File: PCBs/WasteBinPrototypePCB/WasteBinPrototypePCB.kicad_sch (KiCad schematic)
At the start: 31 parts, among them J1 Jack-DC 12V, J2 Conn_01x10_Male, J3 Conn_01x06_Male, J4 SM04B-SRSS-TB(LF)(SN), Q1 MMBT3904, Q2 IRL540NSTRLPBF, U1 PC817, U2 TLV1117-50, U3 ESP32-C3-DEVKITC-02, U4 A1301EUA-T

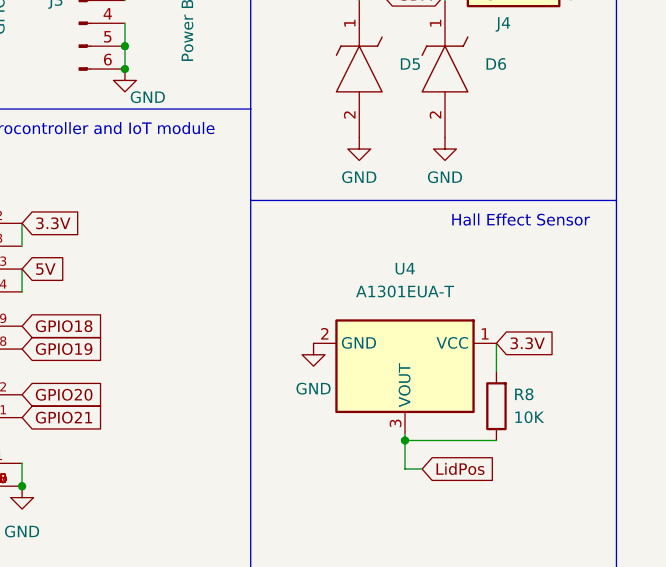
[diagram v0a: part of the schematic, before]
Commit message: footprints assigned to each component
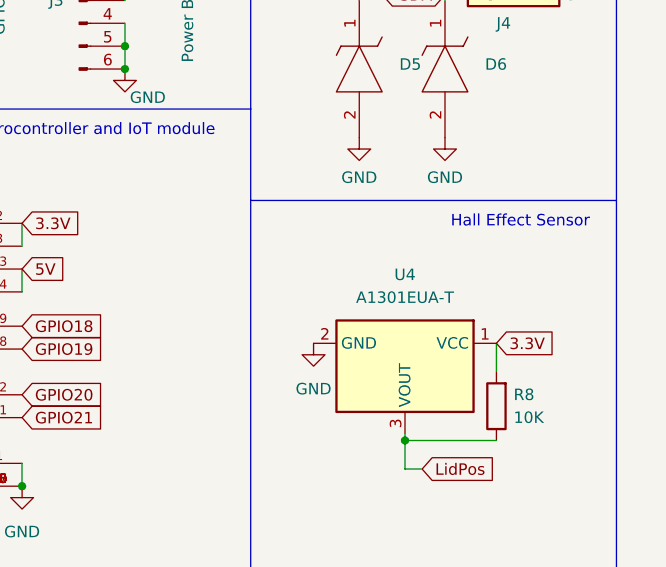
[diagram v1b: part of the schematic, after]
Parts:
- D2: footprint (none) -> LED_SMD:LED_0805_2012Metric_Pad1.15x1.40mm_HandSolder
- D4: footprint (none) -> Diode_SMD:D_0805_2012Metric_Pad1.15x1.40mm_HandSolder; Purpose (none) -> Reverse voltage protection
- J2: footprint (none) -> Connector_PinSocket_2.54mm:PinSocket_1x10_P2.54mm_Vertical
- J3: footprint (none) -> Connector_PinSocket_2.54mm:PinSocket_1x06_P2.54mm_Vertical
- LS1: footprint CMT752580SMTTR -> LED_SMD:LED_0805_2012Metric_Pad1.15x1.40mm_HandSolder
- Q2: footprint IRF2804STRLPBF -> SamacSys_Parts:IRF2804STRLPBF
- R1, R2, R3, R4, R5, R6, R7, R8: footprint (none) -> Resistor_SMD:R_0805_2012Metric_Pad1.20x1.40mm_HandSolder
- U2: footprint (none) -> SamacSys_Parts:SOT230P700X180-4N
- U4: footprint (none) -> Connector_PinSocket_2.54mm:PinSocket_1x03_P2.54mm_Vertical
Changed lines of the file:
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@@
       (effects (font (size 1.27 1.27)) (justify left))
     )
-    (property "Footprint" "IRF2804STRLPBF" (id 2) (at 41.275 45.085 0)
+    (property "Footprint" "SamacSys_Parts:IRF2804STRLPBF" (id 2) (at 41.275 45.085 0)
       (effects (font (size 1.27 1.27)) (justify left) hide)
     )
@@
       (effects (font (size 1.27 1.27)) hide)
     )
-    (property "Footprint" "" (id 2) (at 171.45 29.21 0)
+    (property "Footprint" "Connector_PinSocket_2.54mm:PinSocket_1x06_P2.54mm_Vertical" (id 2) (at 171.45 29.21 0)
       (effects (font (size 1.27 1.27)) hide)
     )
@@
       (effects (font (size 1.27 1.27)) (justify left))
     )
-    (property "Footprint" "" (id 2) (at 52.197 47.625 90)
+    (property "Footprint" "Resistor_SMD:R_0805_2012Metric_Pad1.20x1.40mm_HandSolder" (id 2) (at 52.197 47.625 90)
       (effects (font (size 1.27 1.27)) hide)
     )
@@
       (effects (font (size 1.27 1.27)) (justify right))
     )
-    (property "Footprint" "" (id 2) (at 219.583 74.295 90)
+    (property "Footprint" "Resistor_SMD:R_0805_2012Metric_Pad1.20x1.40mm_HandSolder" (id 2) (at 219.583 74.295 90)
       (effects (font (size 1.27 1.27)) hide)
     )
@@
       (effects (font (size 1.27 1.27)) (justify left))
     )
-    (property "Footprint" "" (id 2) (at 67.31 47.625 0)
+    (property "Footprint" "Diode_SMD:D_0805_2012Metric_Pad1.15x1.40mm_HandSolder" (id 2) (at 67.31 47.625 0)
       (effects (font (size 1.27 1.27)) hide)
     )
     (property "Datasheet" "~" (id 3) (at 67.31 47.625 0)
+      (effects (font (size 1.27 1.27)) hide)
+    )
+    (property "Purpose" "Reverse voltage protection " (id 4) (at 67.31 47.625 0)
       (effects (font (size 1.27 1.27)) hide)
     )
@@
     (property "Reference" "R5" (id 0) (at 59.69 38.1 90))
     (property "Value" "100" (id 1) (at 59.69 40.64 90))
-    (property "Footprint" "" (id 2) (at 59.69 45.593 90)
+    (property "Footprint" "Resistor_SMD:R_0805_2012Metric_Pad1.20x1.40mm_HandSolder" (id 2) (at 59.69 45.593 90)
       (effects (font (size 1.27 1.27)) hide)
     )
@@
       (effects (font (size 1.27 1.27)) (justify right))
     )
-    (property "Footprint" "" (id 2) (at 46.863 72.39 90)
+    (property "Footprint" "Resistor_SMD:R_0805_2012Metric_Pad1.20x1.40mm_HandSolder" (id 2) (at 46.863 72.39 90)
       (effects (font (size 1.27 1.27)) hide)
     )
@@
       (effects (font (size 1.27 1.27)) (justify left))
     )
-    (property "Footprint" "" (id 2) (at 65.532 24.765 90)
+    (property "Footprint" "Resistor_SMD:R_0805_2012Metric_Pad1.20x1.40mm_HandSolder" (id 2) (at 65.532 24.765 90)
       (effects (font (size 1.27 1.27)) hide)
     )
@@
     (property "Reference" "R1" (id 0) (at 41.275 78.105 90))
     (property "Value" "1K" (id 1) (at 41.275 80.645 90))
-    (property "Footprint" "" (id 2) (at 41.275 85.598 90)
+    (property "Footprint" "Resistor_SMD:R_0805_2012Metric_Pad1.20x1.40mm_HandSolder" (id 2) (at 41.275 85.598 90)
       (effects (font (size 1.27 1.27)) hide)
     )
@@
       (effects (font (size 1.27 1.27)) (justify left))
     )
-    (property "Footprint" "" (id 2) (at 43.307 29.21 90)
+    (property "Footprint" "Resistor_SMD:R_0805_2012Metric_Pad1.20x1.40mm_HandSolder" (id 2) (at 43.307 29.21 90)
       (effects (font (size 1.27 1.27)) hide)
     )
@@
     (property "Reference" "LS1" (id 0) (at 67.945 63.5 0))
     (property "Value" "CMT-7525-80-SMT-TR" (id 1) (at 67.945 66.04 0))
-    (property "Footprint" "CMT752580SMTTR" (id 2) (at 78.105 69.215 0)
+    (property "Footprint" "LED_SMD:LED_0805_2012Metric_Pad1.15x1.40mm_HandSolder" (id 2) (at 78.105 69.215 0)
       (effects (font (size 1.27 1.27)) (justify left) hide)
     )
@@
       (effects (font (size 1.27 1.27)) hide)
     )
-    (property "Footprint" "" (id 2) (at 146.05 26.67 0)
+    (property "Footprint" "Connector_PinSocket_2.54mm:PinSocket_1x10_P2.54mm_Vertical" (id 2) (at 146.05 26.67 0)
       (effects (font (size 1.27 1.27)) hide)
     )
@@
   (symbol (lib_id "Sensor_Magnetic:A1301EUA-T") (at 207.645 69.85 270) (unit 1)
     (in_bom yes) (on_board yes) (fields_autoplaced)
-    (property "Reference" "U4" (id 0) (at 207.645 59.055 90))
-    (property "Value" "A1301EUA-T" (id 1) (at 207.645 61.595 90))
-    (property "Footprint" "" (id 2) (at 198.755 69.85 0)
+    (property "Reference" "U4" (id 0) (at 207.645 59.69 90))
+    (property "Value" "A1301EUA-T" (id 1) (at 207.645 62.23 90))
+    (property "Footprint" "Connector_PinSocket_2.54mm:PinSocket_1x03_P2.54mm_Vertical" (id 2) (at 198.755 69.85 0)
       (effects (font (size 1.27 1.27) italic) (justify left) hide)
     )
@@
     (property "Reference" "U2" (id 0) (at 120.65 17.145 0))
     (property "Value" "TLV1117-50" (id 1) (at 120.65 19.685 0))
-    (property "Footprint" "" (id 2) (at 120.65 24.13 0)
+    (property "Footprint" "SamacSys_Parts:SOT230P700X180-4N" (id 2) (at 120.65 24.13 0)
       (effects (font (size 1.27 1.27)) hide)
     )
@@
       (effects (font (size 1.27 1.27)) (justify right))
     )
-    (property "Footprint" "" (id 2) (at 45.085 20.32 0)
+    (property "Footprint" "LED_SMD:LED_0805_2012Metric_Pad1.15x1.40mm_HandSolder" (id 2) (at 45.085 20.32 0)
       (effects (font (size 1.27 1.27)) hide)
     )
@@
     (property "Reference" "R7" (id 0) (at 86.36 29.21 90))
     (property "Value" "1K" (id 1) (at 86.36 31.75 90))
-    (property "Footprint" "" (id 2) (at 86.36 37.338 90)
+    (property "Footprint" "Resistor_SMD:R_0805_2012Metric_Pad1.20x1.40mm_HandSolder" (id 2) (at 86.36 37.338 90)
       (effects (font (size 1.27 1.27)) hide)
     )
@@
     )
     (path "/f387ffcc-26b6-418e-82fe-9f2886ad1d96"
-      (reference "D2") (unit 1) (value "LED") (footprint "")
+      (reference "D2") (unit 1) (value "LED") (footprint "LED_SMD:LED_0805_2012Metric_Pad1.15x1.40mm_HandSolder")
     )
     (path "/3b6822c2-ef43-441b-ada3-a919003dfb41"
@@
     )
     (path "/2daceb28-157a-44a8-abe7-ecdcfa40433f"
-      (reference "D4") (unit 1) (value "D") (footprint "")
+      (reference "D4") (unit 1) (value "D") (footprint "Diode_SMD:D_0805_2012Metric_Pad1.15x1.40mm_HandSolder")
     )
     (path "/de6b862e-7ecd-43af-9a8b-58b048cb163f"
@@
     )
     (path "/ba6425fc-a624-41b4-91aa-0f0a86e87413"
-      (reference "J2") (unit 1) (value "Conn_01x10_Male") (footprint "")
+      (reference "J2") (unit 1) (value "Conn_01x10_Male") (footprint "Connector_PinSocket_2.54mm:PinSocket_1x10_P2.54mm_Vertical")
     )
     (path "/1886b725-a5c3-4ddc-8a4b-0787c5600503"
-      (reference "J3") (unit 1) (value "Conn_01x06_Male") (footprint "")
+      (reference "J3") (unit 1) (value "Conn_01x06_Male") (footprint "Connector_PinSocket_2.54mm:PinSocket_1x06_P2.54mm_Vertical")
     )
     (path "/48eea9cc-6ff2-4ff5-8e23-5348d769bac2"
@@
     )
     (path "/9af62221-658d-49f1-9d88-b604899cb68f"
-      (reference "LS1") (unit 1) (value "CMT-7525-80-SMT-TR") (footprint "CMT752580SMTTR")
+      (reference "LS1") (unit 1) (value "CMT-7525-80-SMT-TR") (footprint "LED_SMD:LED_0805_2012Metric_Pad1.15x1.40mm_HandSolder")
     )
     (path "/6cbf8465-a06f-4c9b-9f77-203331441ebb"
@@
     )
     (path "/00039052-8388-45e9-8681-1233f0361ca2"
-      (reference "Q2") (unit 1) (value "IRL540NSTRLPBF") (footprint "IRF2804STRLPBF")
+      (reference "Q2") (unit 1) (value "IRL540NSTRLPBF") (footprint "SamacSys_Parts:IRF2804STRLPBF")
     )
     (path "/8a915310-eef9-46a2-abfe-017b4243f876"
-      (reference "R1") (unit 1) (value "1K") (footprint "")
+      (reference "R1") (unit 1) (value "1K") (footprint "Resistor_SMD:R_0805_2012Metric_Pad1.20x1.40mm_HandSolder")
     )
     (path "/9a0e7e10-daef-4ecc-9000-f4c879837019"
-      (reference "R2") (unit 1) (value "4.7K") (footprint "")
+      (reference "R2") (unit 1) (value "4.7K") (footprint "Resistor_SMD:R_0805_2012Metric_Pad1.20x1.40mm_HandSolder")
     )
     (path "/6ac53d1d-5b54-436c-a17c-2b8eabcb5fb8"
-      (reference "R3") (unit 1) (value "1K") (footprint "")
+      (reference "R3") (unit 1) (value "1K") (footprint "Resistor_SMD:R_0805_2012Metric_Pad1.20x1.40mm_HandSolder")
     )
     (path "/1d4a2c9b-4688-4ac1-a0f6-6d53ea4c195a"
-      (reference "R4") (unit 1) (value "4.7K") (footprint "")
+      (reference "R4") (unit 1) (value "4.7K") (footprint "Resistor_SMD:R_0805_2012Metric_Pad1.20x1.40mm_HandSolder")
     )
     (path "/4583b515-ed49-4672-843a-9aa019653137"
-      (reference "R5") (unit 1) (value "100") (footprint "")
+      (reference "R5") (unit 1) (value "100") (footprint "Resistor_SMD:R_0805_2012Metric_Pad1.20x1.40mm_HandSolder")
     )
     (path "/8392ea61-db32-4e4d-98fb-bb6a7b8732c6"
-      (reference "R6") (unit 1) (value "4.7K") (footprint "")
+      (reference "R6") (unit 1) (value "4.7K") (footprint "Resistor_SMD:R_0805_2012Metric_Pad1.20x1.40mm_HandSolder")
     )
     (path "/f92dea4e-1671-4b54-9938-25a37f0f0f25"
-      (reference "R7") (unit 1) (value "1K") (footprint "")
+      (reference "R7") (unit 1) (value "1K") (footprint "Resistor_SMD:R_0805_2012Metric_Pad1.20x1.40mm_HandSolder")
     )
     (path "/23a0a120-4468-43ee-9d86-86770507e5ab"
-      (reference "R8") (unit 1) (value "10K") (footprint "")
+      (reference "R8") (unit 1) (value "10K") (footprint "Resistor_SMD:R_0805_2012Metric_Pad1.20x1.40mm_HandSolder")
     )
     (path "/6da0c24a-8f42-4cc5-8456-4753040ff7fb"
@@
     )
     (path "/e1f7d1f4-cb75-4a16-a424-ceb6b194750c"
-      (reference "U2") (unit 1) (value "TLV1117-50") (footprint "")
+      (reference "U2") (unit 1) (value "TLV1117-50") (footprint "SamacSys_Parts:SOT230P700X180-4N")
     )
     (path "/f6a6228d-b0a5-48ac-a9fa-75e45ef281d6"
@@
     )
     (path "/d6911078-c811-4b16-81c1-2d59c3e06949"
-      (reference "U4") (unit 1) (value "A1301EUA-T") (footprint "")
-    )
-  )
+      (reference "U4") (unit 1) (value "A1301EUA-T") (footprint "Connector_PinSocket_2.54mm:PinSocket_1x03_P2.54mm_Vertical")
+    )
+  )

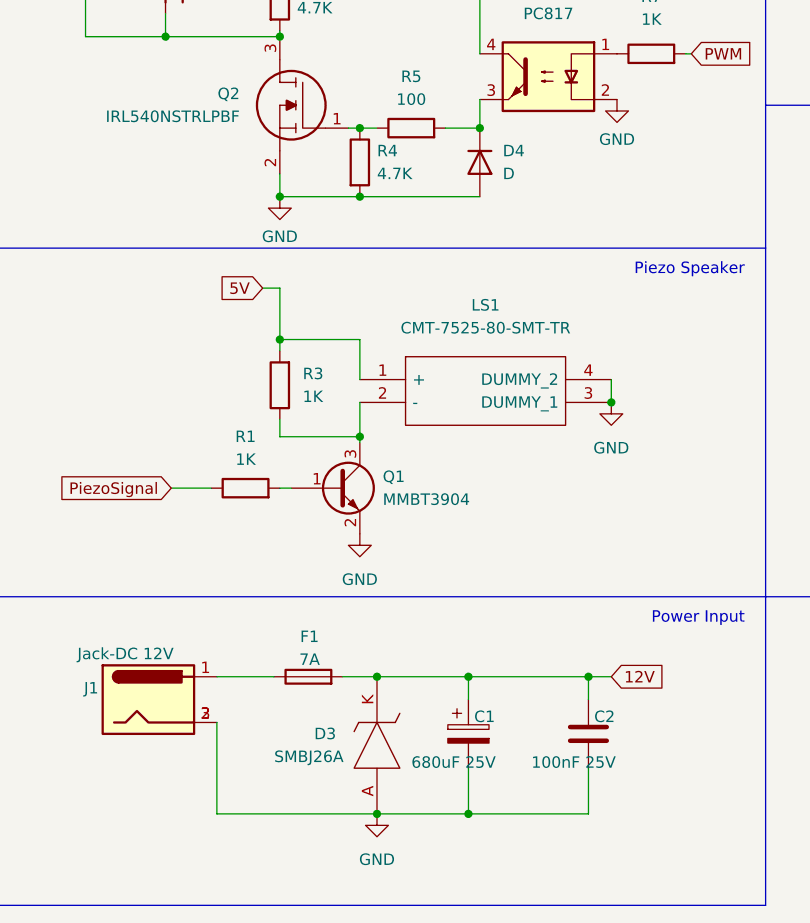
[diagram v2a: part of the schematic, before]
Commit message: grouped componentes
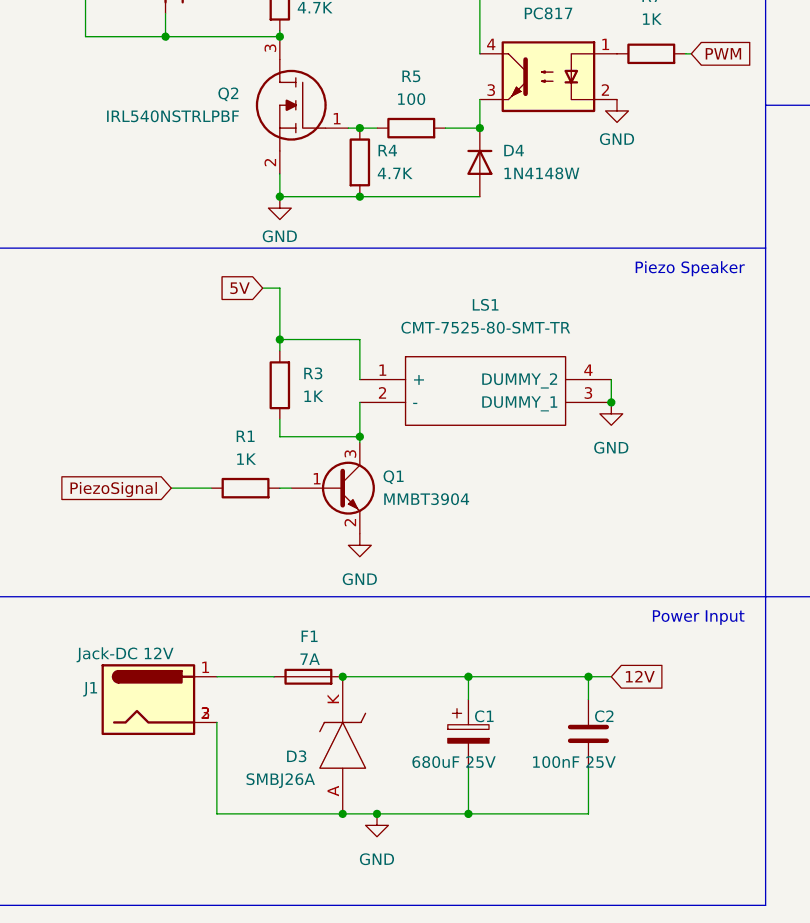
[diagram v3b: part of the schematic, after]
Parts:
- D4: value D -> 1N4148W; footprint Diode_SMD:D_0805_2012Metric_Pad1.15x1.40mm_HandSolder -> Diode_SMD:D_SOD-123
- LS1: footprint LED_SMD:LED_0805_2012Metric_Pad1.15x1.40mm_HandSolder -> SamacSys_Parts:CMT752580SMTTR
- PE1: footprint SamacSys_Parts:1808190 -> TerminalBlock:TerminalBlock_bornier-2_P5.08mm
